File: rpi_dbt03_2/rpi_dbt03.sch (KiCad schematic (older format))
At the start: 33 parts, among them J2 Conn_02x03_Odd_Even, Q1 BC546, U1 ATmega8L-8PU, U2 SFH617A-1, U3 SFH617A-1, U4 SFH617A-1, Y1 8MHz

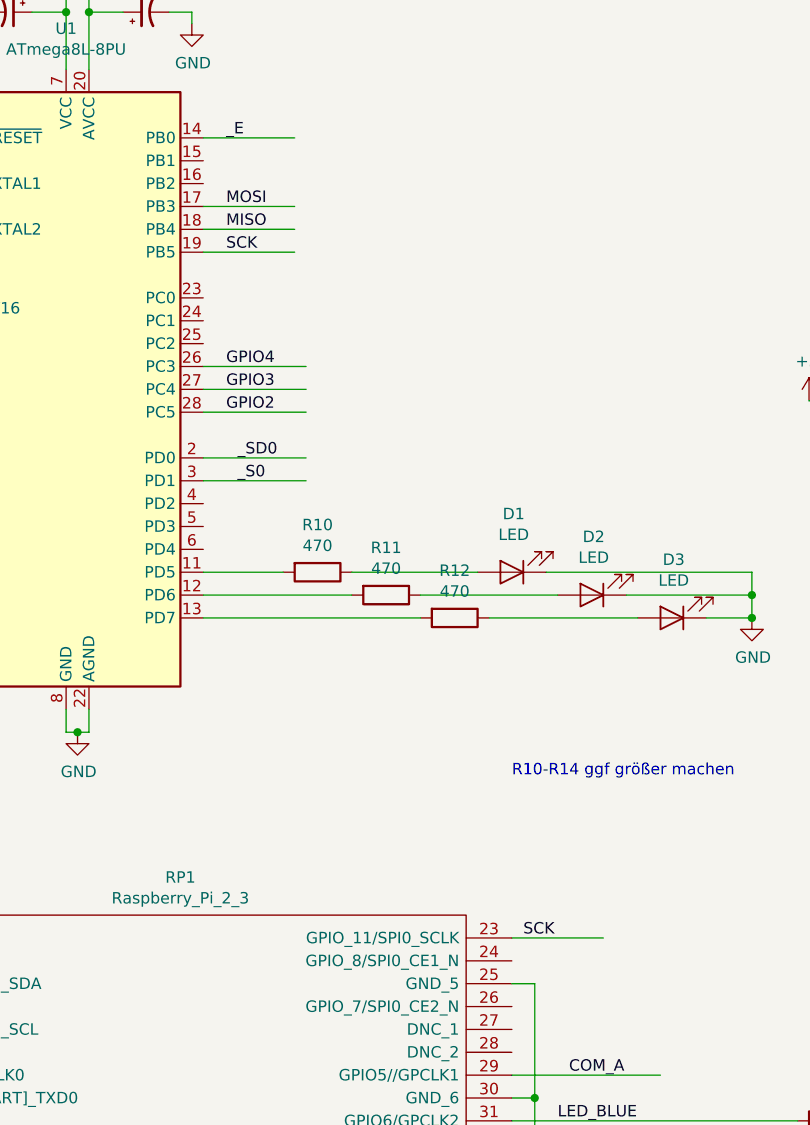
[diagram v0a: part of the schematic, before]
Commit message: Found a hardware Bug. Pin 18 of the ATMega8 needs to connected to Pin 24 of the Raspberry PI. This will mean that a new layout is needed, however so far you can patch it by adding one bodge wire.
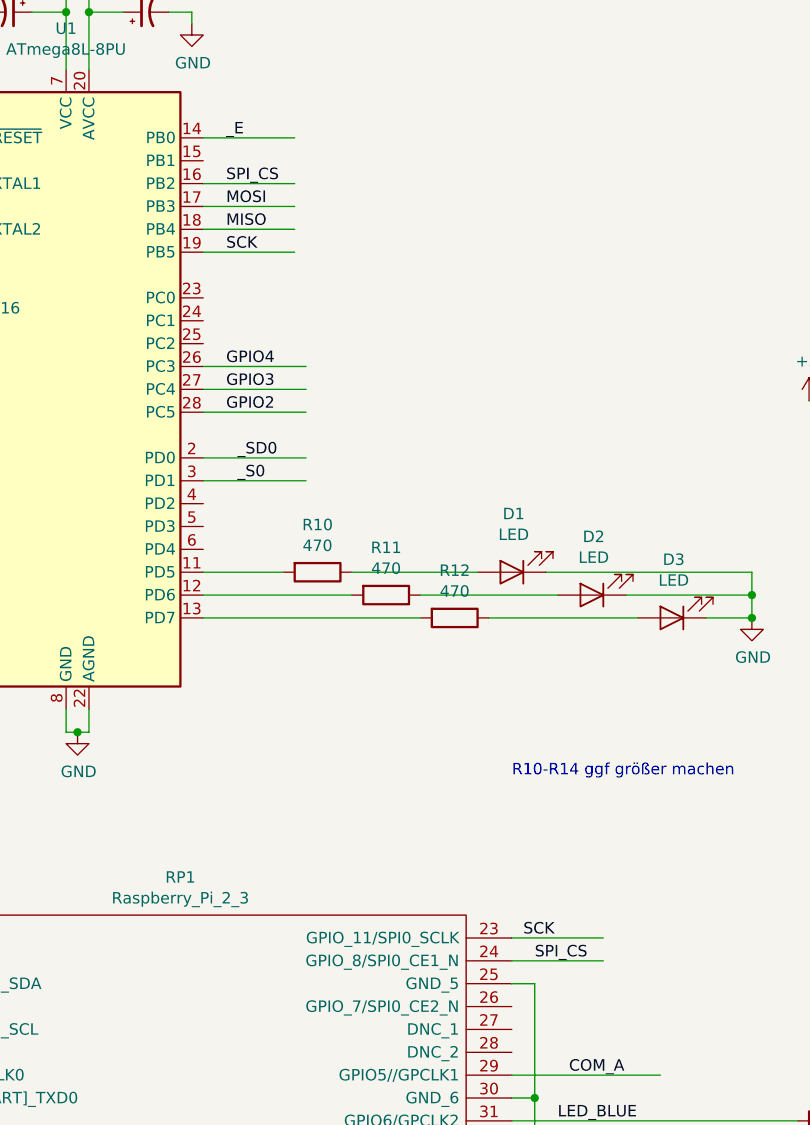
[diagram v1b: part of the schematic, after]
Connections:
- net labels added: SPI_CS
- wire segments 148 -> 150
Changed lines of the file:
@@
 Text Notes 4900 4200 0    50   ~ 0
 R10-R14 ggf größer machen
+Wire Wire Line
+	3550 1600 3950 1600
+Text Label 3650 1600 0    50   ~ 0
+SPI_CS
+Wire Wire Line
+	4900 5000 5300 5000
+Text Label 5000 5000 0    50   ~ 0
+SPI_CS
 $EndSCHEMATC

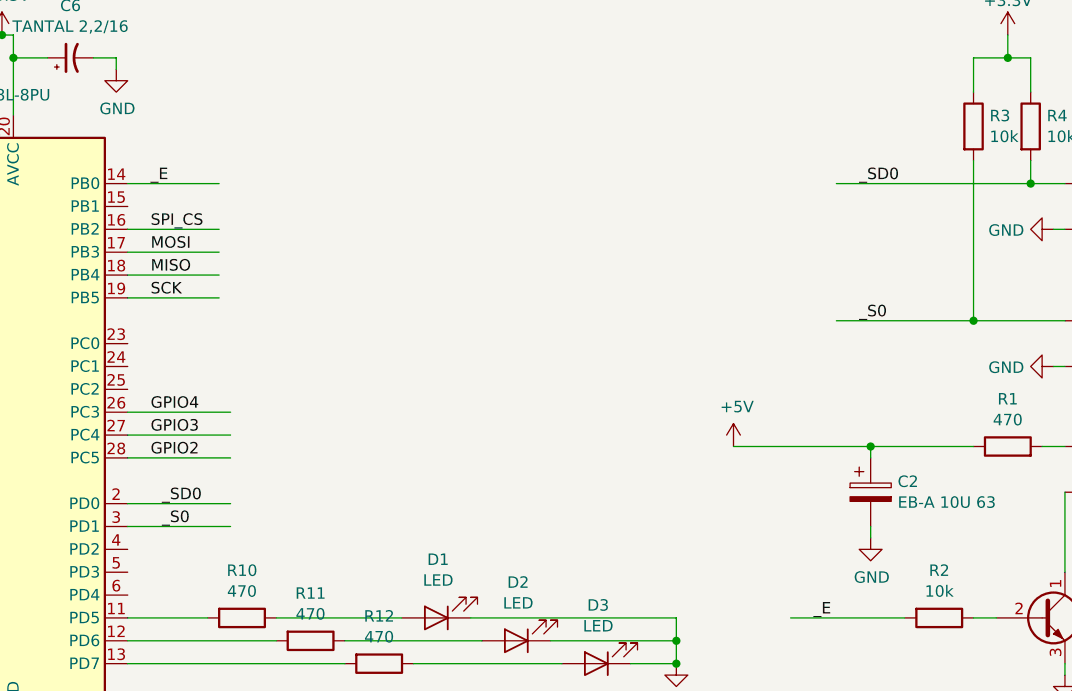
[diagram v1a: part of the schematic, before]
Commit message: Added SPI_CE line and swapped incorrectly named _SD0 and _S0 netw
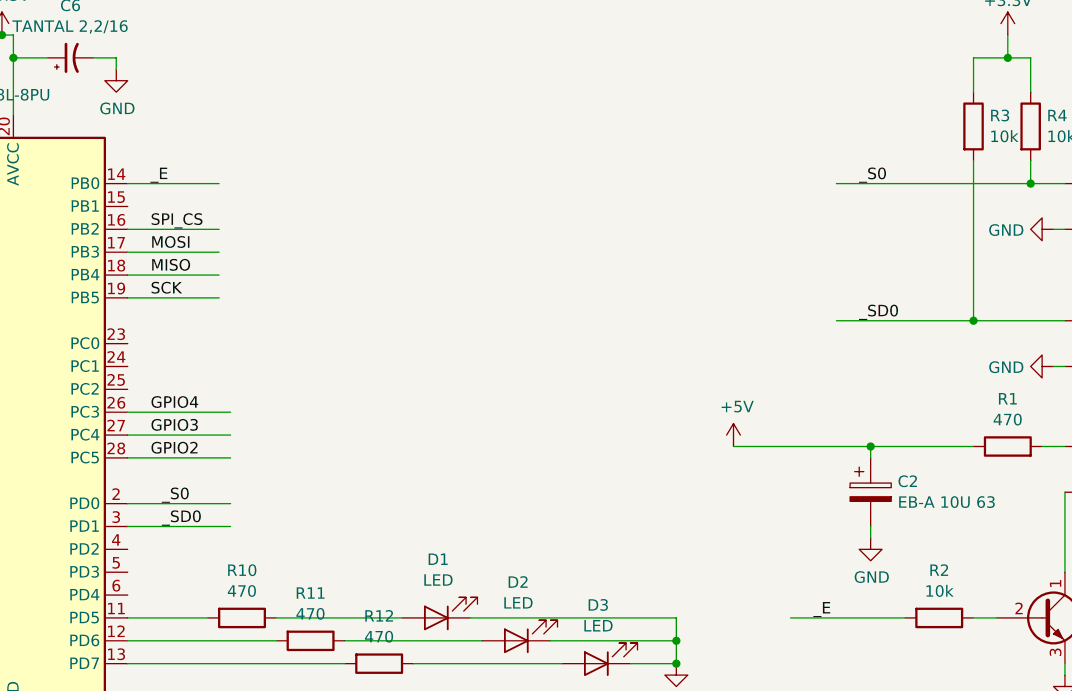
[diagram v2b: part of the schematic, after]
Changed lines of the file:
@@
 Text Label 3650 1400 0    50   ~ 0
 _E
-Text Label 3700 2800 0    50   ~ 0
-_SD0
-Text Label 3700 2900 0    50   ~ 0
-_S0
-Text Label 6750 1400 0    50   ~ 0
-_SD0
-Text Label 6750 2000 0    50   ~ 0
-_S0
 Text Label 6550 3300 0    50   ~ 0
 _E
@@
 Text Label 5000 5000 0    50   ~ 0
 SPI_CS
+Text Label 6750 1400 0    50   ~ 0
+_S0
+Text Label 6750 2000 0    50   ~ 0
+_SD0
+Text Label 3700 2800 0    50   ~ 0
+_S0
+Text Label 3700 2900 0    50   ~ 0
+_SD0
 $EndSCHEMATC

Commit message: Version 3 which adds 3 buttons and some configuration jumpers
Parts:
- removed R7: 2k2, Resistors_ThroughHole:R_Axial_DIN0207_L6.3mm_D2.5mm_P7.62mm_Horizontal, symbol Device:R
- added J1: Conn_02x02_Counter_Clockwise, Pin_Headers:Pin_Header_Straight_2x02_Pitch2.54mm, symbol Connector_Generic:Conn_02x02_Counter_Clockwise
- added SW1, SW2, SW3: SW_Push, Buttons_Switches_ThroughHole:SW_PUSH_6mm, symbol Switch:SW_Push
- C6: footprint Capacitors_ThroughHole:CP_Radial_Tantal_D4.5mm_P2.50mm -> Capacitors_ThroughHole:C_Disc_D3.0mm_W2.0mm_P2.50mm
- R10, R11, R12: value 470 -> 2k2
- U1: symbol MCU_Microchip_ATmega:ATmega8L-8PU -> rpi_dbt03-rescue:ATmega8L-8PU-MCU_Microchip_ATmega
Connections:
- net labels added: GPIO14, GPIO15, GPIO17
- wire segments 150 -> 164
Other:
- note added: "3"
- note removed: "R10-R14 ggf größer machen"
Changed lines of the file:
@@
 EESchema Schematic File Version 4
-LIBS:rpi_dbt03-cache
-EELAYER 26 0
+EELAYER 30 0
 EELAYER END
 $Descr A4 11693 8268
@@
 	0    1    1    0
 $EndComp
-$Comp
-L Device:R R7
-U 1 1 5E0D1AD8
-P 9000 2350
-F 0 "R7" H 9070 2396 50  0000 L CNN
-F 1 "2k2" H 9070 2305 50  0000 L CNN
-F 2 "Resistors_ThroughHole:R_Axial_DIN0207_L6.3mm_D2.5mm_P7.62mm_Horizontal" V 8930 2350 50  0001 C CNN
-F 3 "~" H 9000 2350 50  0001 C CNN
-	1    9000 2350
-	1    0    0    -1
-$EndComp
-Wire Wire Line
-	9000 2550 9000 2500
-Wire Wire Line
-	8850 1400 9000 1400
 Wire Wire Line
 	8250 2200 8350 2200
@@
 Wire Wire Line
 	8250 1400 8550 1400
-Wire Wire Line
-	8250 2550 9000 2550
 Wire Wire Line
 	8250 1600 8350 1600
@@
 Wire Wire Line
 	10800 1400 11000 1400
-Wire Wire Line
-	9000 1400 9000 2200
 Wire Wire Line
 	8250 2000 8450 2000
@@
 	8350 2750 9150 2750
 Connection ~ 8350 2750
-Connection ~ 9000 1400
 Wire Wire Line
 	9300 2000 9300 1600
@@
 Wire Wire Line
 	10450 1700 10700 1700
-Connection ~ 9000 2550
 Wire Wire Line
 	7400 750  7400 850
@@
 $EndComp
 Wire Wire Line
-	2000 5900 1400 5900
-Wire Wire Line
-	2000 6100 1400 6100
-Wire Wire Line
 	2000 6300 1400 6300
 Wire Wire Line
@@
 ED0
 $Comp
-L MCU_Microchip_ATmega:ATmega8L-8PU U1
+L rpi_dbt03-rescue:ATmega8L-8PU-MCU_Microchip_ATmega U1
 U 1 1 5E3A2415
 P 2950 2500
@@
 $EndComp
 Wire Wire Line
-	9000 1400 10200 1400
-Wire Wire Line
 	9300 1600 10200 1600
-Wire Wire Line
-	9000 2550 11000 2550
 $Comp
 L Device:Crystal_Small Y1
@@
 Wire Wire Line
 	2950 750  3000 750
-Wire Wire Line
-	3050 750  3050 850
 $Comp
 L power:+3.3V #PWR0110
@@
 SCK
 $Comp
-L Device:CP1_Small C6
-U 1 1 5E3E601C
-P 3300 850
-F 0 "C6" V 3528 850 50  0000 C CNN
-F 1 "TANTAL 2,2/16" V 3437 850 50  0000 C CNN
-F 2 "Capacitors_ThroughHole:CP_Radial_Tantal_D4.5mm_P2.50mm" H 3300 850 50  0001 C CNN
-F 3 "~" H 3300 850 50  0001 C CNN
-	1    3300 850
-	0    -1   -1   0
-$EndComp
-$Comp
 L Device:CP1_Small C5
 U 1 1 5E3E6195
@@
 	2950 850  2950 750
 Wire Wire Line
-	3050 850  3200 850
-Connection ~ 3050 850
-Wire Wire Line
-	3050 850  3050 1100
-$Comp
-L Device:CP1_Small C4
-U 1 1 5E3EED0B
-P 2150 2100
-F 0 "C4" H 2241 2146 50  0000 L CNN
-F 1 "TANTAL 2,2/16" H 2241 2055 50  0000 L CNN
-F 2 "Capacitors_ThroughHole:CP_Radial_Tantal_D4.5mm_P2.50mm" H 2150 2100 50  0001 C CNN
-F 3 "~" H 2150 2100 50  0001 C CNN
-	1    2150 2100
-	1    0    0    -1
-$EndComp
-Wire Wire Line
 	2350 2000 2150 2000
 $Comp
@@
 $EndComp
 $Comp
-L power:GND #PWR0113
-U 1 1 5E3F38C3
-P 3500 900
-F 0 "#PWR0113" H 3500 650 50  0001 C CNN
-F 1 "GND" H 3505 727 50  0000 C CNN
-F 2 "" H 3500 900 50  0001 C CNN
-F 3 "" H 3500 900 50  0001 C CNN
-	1    3500 900
-	1    0    0    -1
-$EndComp
-$Comp
 L power:GND #PWR0114
 U 1 1 5E3F393C
@@
 	2500 850  2500 900
 Wire Wire Line
-	3400 850  3500 850
-Wire Wire Line
-	3500 850  3500 900
-Wire Wire Line
 	2150 2200 2150 2300
 Wire Wire Line
@@
 Wire Wire Line
 	3550 2500 4000 2500
-Wire Wire Line
-	3550 2400 4000 2400
 Wire Wire Line
 	2000 5100 1400 5100
@@
 Text Label 3650 2500 0    50   ~ 0
 GPIO3
-Text Label 3650 2400 0    50   ~ 0
-GPIO4
 $Comp
 L Device:R R9
@@
 P 4050 3300
 F 0 "R10" V 3843 3300 50  0000 C CNN
-F 1 "470" V 3934 3300 50  0000 C CNN
+F 1 "2k2" V 3934 3300 50  0000 C CNN
 F 2 "Resistors_ThroughHole:R_Axial_DIN0207_L6.3mm_D2.5mm_P7.62mm_Horizontal" V 3980 3300 50  0001 C CNN
 F 3 "~" H 4050 3300 50  0001 C CNN
@@
 P 4350 3400
 F 0 "R11" V 4143 3400 50  0000 C CNN
-F 1 "470" V 4234 3400 50  0000 C CNN
+F 1 "2k2" V 4234 3400 50  0000 C CNN
 F 2 "Resistors_ThroughHole:R_Axial_DIN0207_L6.3mm_D2.5mm_P7.62mm_Horizontal" V 4280 3400 50  0001 C CNN
 F 3 "~" H 4350 3400 50  0001 C CNN
@@
 P 4650 3500
 F 0 "R12" V 4443 3500 50  0000 C CNN
-F 1 "470" V 4534 3500 50  0000 C CNN
+F 1 "2k2" V 4534 3500 50  0000 C CNN
 F 2 "Resistors_ThroughHole:R_Axial_DIN0207_L6.3mm_D2.5mm_P7.62mm_Horizontal" V 4580 3500 50  0001 C CNN
 F 3 "~" H 4650 3500 50  0001 C CNN
@@
 Text Notes 7400 7500 0    50   ~ 0
 RPI to DBT-03
-Text Notes 4900 4200 0    50   ~ 0
-R10-R14 ggf größer machen
 Wire Wire Line
 	3550 1600 3950 1600
@@
 Text Label 3700 2900 0    50   ~ 0
 _SD0
+$Comp
+L Switch:SW_Push SW1
+U 1 1 5EE936A4
+P 10000 4200
+F 0 "SW1" H 10000 4485 50  0000 C CNN
+F 1 "SW_Push" H 10000 4394 50  0000 C CNN
+F 2 "Buttons_Switches_ThroughHole:SW_PUSH_6mm" H 10000 4400 50  0001 C CNN
+F 3 "~" H 10000 4400 50  0001 C CNN
+	1    10000 4200
+	1    0    0    -1
+$EndComp
+$Comp
+L power:GND #PWR0120
+U 1 1 5EE95F9E
+P 10350 5500
+F 0 "#PWR0120" H 10350 5250 50  0001 C CNN
+F 1 "GND" H 10355 5327 50  0000 C CNN
+F 2 "" H 10350 5500 50  0001 C CNN
+F 3 "" H 10350 5500 50  0001 C CNN
+	1    10350 5500
+	1    0    0    -1
+$EndComp
+Wire Wire Line
+	10200 4200 10350 4200
+Wire Wire Line
+	9800 4200 9100 4200
+Text Label 9150 4200 0    50   ~ 0
+GPIO3
+Wire Wire Line
+	8850 1400 10200 1400
+Wire Wire Line
+	8250 2550 11000 2550
+Text Label 1450 5600 0    50   ~ 0
+GPIO14
+Text Label 1450 5800 0    50   ~ 0
+GPIO15
+Text Label 1450 5900 0    50   ~ 0
+GPIO17
+Wire Wire Line
+	2000 6000 1400 6000
+$Comp
+L Connector_Generic:Conn_02x02_Counter_Clockwise J1
+U 1 1 5EEFCF81
+P 1000 5900
+F 0 "J1" H 1050 5575 50  0000 C CNN
+F 1 "Conn_02x02_Counter_Clockwise" H 1050 5666 50  0000 C CNN
+F 2 "Pin_Headers:Pin_Header_Straight_2x02_Pitch2.54mm" H 1000 5900 50  0001 C CNN
+F 3 "~" H 1000 5900 50  0001 C CNN
+	1    1000 5900
+	-1   0    0    1
+$EndComp
+Wire Wire Line
+	1200 5900 2000 5900
+Wire Wire Line
+	1300 6100 1300 5800
+Wire Wire Line
+	1300 5800 1200 5800
+Wire Wire Line
+	1300 6100 2000 6100
+Wire Wire Line
+	1400 5800 1400 5700
+Wire Wire Line
+	1400 5700 700  5700
+Wire Wire Line
+	700  5700 700  5800
+$Comp
+L power:GND #PWR0122
+U 1 1 5EF35B76
+P 650 6000
+F 0 "#PWR0122" H 650 5750 50  0001 C CNN
+F 1 "GND" H 655 5827 50  0000 C CNN
+F 2 "" H 650 6000 50  0001 C CNN
+F 3 "" H 650 6000 50  0001 C CNN
+	1    650  6000
+	1    0    0    -1
+$EndComp
+Wire Wire Line
+	700  5900 650  5900
+Wire Wire Line
+	650  5900 650  6000
+Wire Wire Line
+	3050 750  3050 850
+$Comp
+L Device:CP1_Small C4
+U 1 1 5EF5520E
+P 3400 850
+F 0 "C4" V 3172 850 50  0000 C CNN
+F 1 "TANTAL 2,2/16" V 3263 850 50  0000 C CNN
+F 2 "Capacitors_ThroughHole:CP_Radial_Tantal_D4.5mm_P2.50mm" H 3400 850 50  0001 C CNN
+F 3 "~" H 3400 850 50  0001 C CNN
+	1    3400 850
+	0    -1   -1   0
+$EndComp
+$Comp
+L power:GND #PWR0113
+U 1 1 5EF5577C
+P 3750 950
+F 0 "#PWR0113" H 3750 700 50  0001 C CNN
+F 1 "GND" H 3755 777 50  0000 C CNN
+F 2 "" H 3750 950 50  0001 C CNN
+F 3 "" H 3750 950 50  0001 C CNN
+	1    3750 950
+	1    0    0    -1
+$EndComp
+Wire Wire Line
+	3300 850  3050 850
+Connection ~ 3050 850
+Wire Wire Line
+	3050 850  3050 1100
+Wire Wire Line
+	3500 850  3750 850
+Wire Wire Line
+	3750 850  3750 950
+$Comp
+L Device:CP1_Small C6
+U 1 1 5EF76464
+P 2150 2100
+F 0 "C6" V 1922 2100 50  0000 C CNN
+F 1 "TANTAL 2,2/16" V 2013 2100 50  0000 C CNN
+F 2 "Capacitors_ThroughHole:C_Disc_D3.0mm_W2.0mm_P2.50mm" H 2150 2100 50  0001 C CNN
+F 3 "~" H 2150 2100 50  0001 C CNN
+	1    2150 2100
+	1    0    0    -1
+$EndComp
+$Comp
+L Switch:SW_Push SW2
+U 1 1 5EF814AB
+P 10000 4800
+F 0 "SW2" H 10000 5085 50  0000 C CNN
+F 1 "SW_Push" H 10000 4994 50  0000 C CNN
+F 2 "Buttons_Switches_ThroughHole:SW_PUSH_6mm" H 10000 5000 50  0001 C CNN
+F 3 "~" H 10000 5000 50  0001 C CNN
+	1    10000 4800
+	1    0    0    -1
+$EndComp
+$Comp
+L Switch:SW_Push SW3
+U 1 1 5EF81E52
+P 10000 5350
+F 0 "SW3" H 10000 5635 50  0000 C CNN
+F 1 "SW_Push" H 10000 5544 50  0000 C CNN
+F 2 "Buttons_Switches_ThroughHole:SW_PUSH_6mm" H 10000 5550 50  0001 C CNN
+F 3 "~" H 10000 5550 50  0001 C CNN
+	1    10000 5350
+	1    0    0    -1
+$EndComp
+Wire Wire Line
+	10350 4200 10350 4800
+Wire Wire Line
+	10200 4800 10350 4800
+Connection ~ 10350 4800
+Wire Wire Line
+	10350 4800 10350 5350
+Wire Wire Line
+	10200 5350 10350 5350
+Connection ~ 10350 5350
+Wire Wire Line
+	10350 5350 10350 5500
+Wire Wire Line
+	9800 4800 9100 4800
+Wire Wire Line
+	9800 5350 9100 5350
+Text Label 9200 4800 0    50   ~ 0
+GPIO4
+Text Label 9200 5350 0    50   ~ 0
+GPIO14
+Wire Wire Line
+	3550 2100 3950 2100
+Wire Wire Line
+	3550 2200 4000 2200
+Text Label 3650 2100 0    50   ~ 0
+GPIO15
+Text Label 3650 2200 0    50   ~ 0
+GPIO17
+Text Notes 10600 7650 0    50   ~ 0
+3
 $EndSCHEMATC
